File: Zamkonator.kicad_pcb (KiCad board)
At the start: 2 copper layers, 75 x 75 mm, 104 parts, among them J1 Screw_Terminal_01x06, J2 RJ45_Abracon_ARJP11A-MASA-B-A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, J3 Conn_01x08_Male, J4 Conn_02x08_Counter_Clockwise, K1 SRD-DC3V-SL-C, Q1 BCP56, T1 HR051142, U1 RTL8201F, U2 SI3404-A-GM, U3 EL3H7-G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

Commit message: Finish layout
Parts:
- added JP1: SolderJumper_2_Open, Jumper:SolderJumper-2_P1.3mm_Open_RoundedPad1.0x1.5mm, B.Cu at (22.5, 72.8)
- added R32: R, Resistor_SMD:R_0603_1608Metric_Pad0.98x0.95mm_HandSolder, F.Cu at (6.00, 31.2)
- J4: value Conn_02x08_Counter_Clockwise -> Conn_02x06_Counter_Clockwise; footprint Connector_PinHeader_2.54mm:PinHeader_2x08_P2.54mm_Vertical -> Connector_PinHeader_2.54mm:PinHeader_2x06_P2.54mm_Vertical
- moved D9 72.6 mm to (15.0, 62.3), turned to 0 degrees
- moved R2 68.6 mm to (72.3, 31.6)
- moved J1 67.5 mm to (3.60, 35.6), turned to -90 degrees
- moved D8 66.8 mm to (3.50, 55.6)
- moved R1 63.9 mm to (72.2, 33.4), turned to 180 degrees
- moved R29 61.9 mm to (7.70, 52.5), turned to 90 degrees
- moved R28 61.8 mm to (19.2, 45.6), turned to 180 degrees
- moved R30 61.7 mm to (23.4, 54.2), turned to 90 degrees
- moved J_LATCH1 60.7 mm to (4.00, 12.0), turned to -90 degrees
- moved C3 55.6 mm to (66.4, 31.5), turned to 0 degrees
- moved R31 55.1 mm to (10.1, 45.6), turned to 180 degrees
- moved U7 54.0 mm to (15.0, 39.0), turned to 180 degrees
- moved U8 53.2 mm to (15.0, 52.0), turned to 0 degrees
- moved C29 52.7 mm to (25.4, 45.5)
- moved C30 52.7 mm to (30.4, 52.2)
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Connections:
- J1 pad 1: +12V -> /Wigand Intrerface/READER_LED
- J1 pad 2: GND -> /Wigand Intrerface/READER_BUZZER
- J1 pad 5: /Wigand Intrerface/READER_LED -> +12V
- J1 pad 6: /Wigand Intrerface/READER_BUZZER -> GND
- J3 pad 3: /ESP32/IO35 -> /ESP32/IO18
- J4 pad 1: /ESP32/IO2 -> /ESP32/IO12
- J4 pad 10: GND -> /ESP32/IO13
- J4 pad 11: +3.3V -> /ESP32/IO5
- J4 pad 12: +3.3V -> /ESP32/IO4
- J4 pad 2: /50MHZ CLOCK/CLK_EN -> /ESP32/IO2
- J4 pad 3: /ESP32/IO5 -> Net-(J4-Pad3)
- J4 pad 4: /ESP32/IO12 -> +3.3V
- J4 pad 5: /ESP32/IO13 -> +3.3V
- J4 pad 6: /ESP32/IO14 -> GND
- J4 pad 8: /ESP32/IO18 -> /50MHZ CLOCK/CLK_EN
- J4 pad 9: GND -> /ESP32/IO23
- Q1 pad 1: /ESP32/IO35 -> Net-(Q1-Pad1)
- R26 pad 1: /ESP32/IO34 -> /ESP32/IO2
- R27 pad 1: /ESP32/IO33 -> /ESP32/IO12
- R28 pad 2: /ESP32/IO32 -> /ESP32/IO13
- U6 pad 13: /ESP32/IO14 -> /50MHZ CLOCK/CLK_EN
- U6 pad 26: /50MHZ CLOCK/CLK_EN -> /ESP32/IO4
- U6 pad 6: /ESP32/IO34 -> unconnected-(U6-Pad6)
- U6 pad 7: /ESP32/IO35 -> unconnected-(U6-Pad7)
- U6 pad 8: /ESP32/IO32 -> unconnected-(U6-Pad8)
- U6 pad 9: /ESP32/IO33 -> unconnected-(U6-Pad9)
- U8 pad 8: /ESP32/IO32 -> /ESP32/IO13
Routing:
- net GND: track 0.00 -> 89.4 mm, vias 0 -> 58
- net /ESP32/IO12: track 4.76 -> 91.3 mm, vias 1 -> 2
- net /ESP32/IO18: track 10.2 -> 94.8 mm, vias 1 -> 4
- net /ESP32/IO13: track 8.83 -> 83.7 mm, vias 1 -> 6
- net VSS: track 66.2 -> 4.53 mm, vias 2 -> 10
- net /ESP32/IO32: track 61.5 -> 0.00 mm, vias 3 -> 0
- net /ESP32/IO35: track 58.8 -> 0.00 mm, vias 2 -> 0
- net /ESP32/EMAC_CRS_DV: track 62.0 -> 12.3 mm, vias 2 -> 0
- net /ESP32/EMAC_RXD1: track 67.9 -> 24.0 mm, vias 2 -> 0
- net /ESP32/IO2: track 19.1 -> 62.3 mm, vias 1 -> 2
- net +12V: track 172.7 -> 130.5 mm
- net +3.3V: track 218.6 -> 260.5 mm, vias 4 -> 6
- net /50MHZ CLOCK/CLK_OUT: track 90.3 -> 49.5 mm
- net /ESP32/EMAC_RXD0: track 67.4 -> 27.2 mm, vias 2 -> 0
- net Net-(R1-Pad2): track 56.0 -> 16.9 mm
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- added copper zone on B.Cu, net GND
- added copper zone on F.Cu, net GND
- added copper zone on B.Cu, net VSS
- added copper zone on F.Cu, net VSS
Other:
- outline, holes or cut-outs redrawn

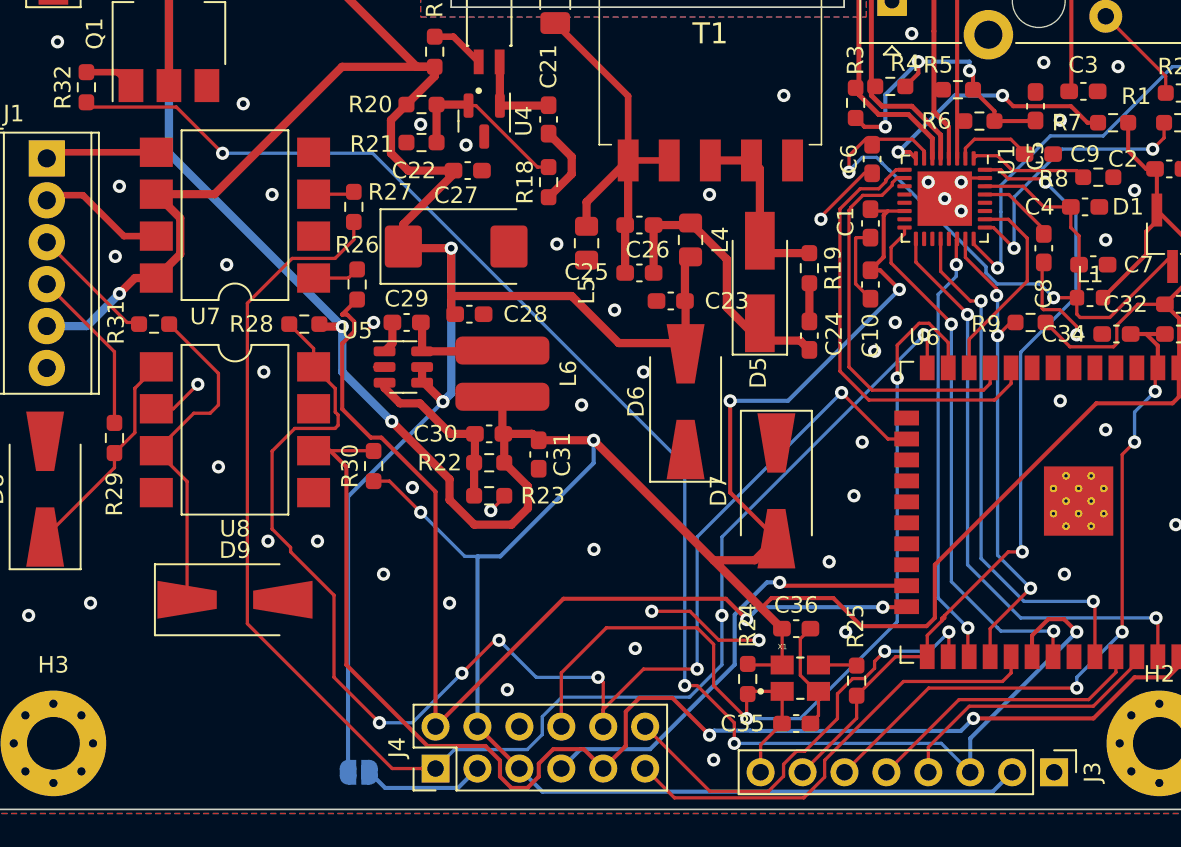
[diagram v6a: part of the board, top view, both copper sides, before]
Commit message: add header labels
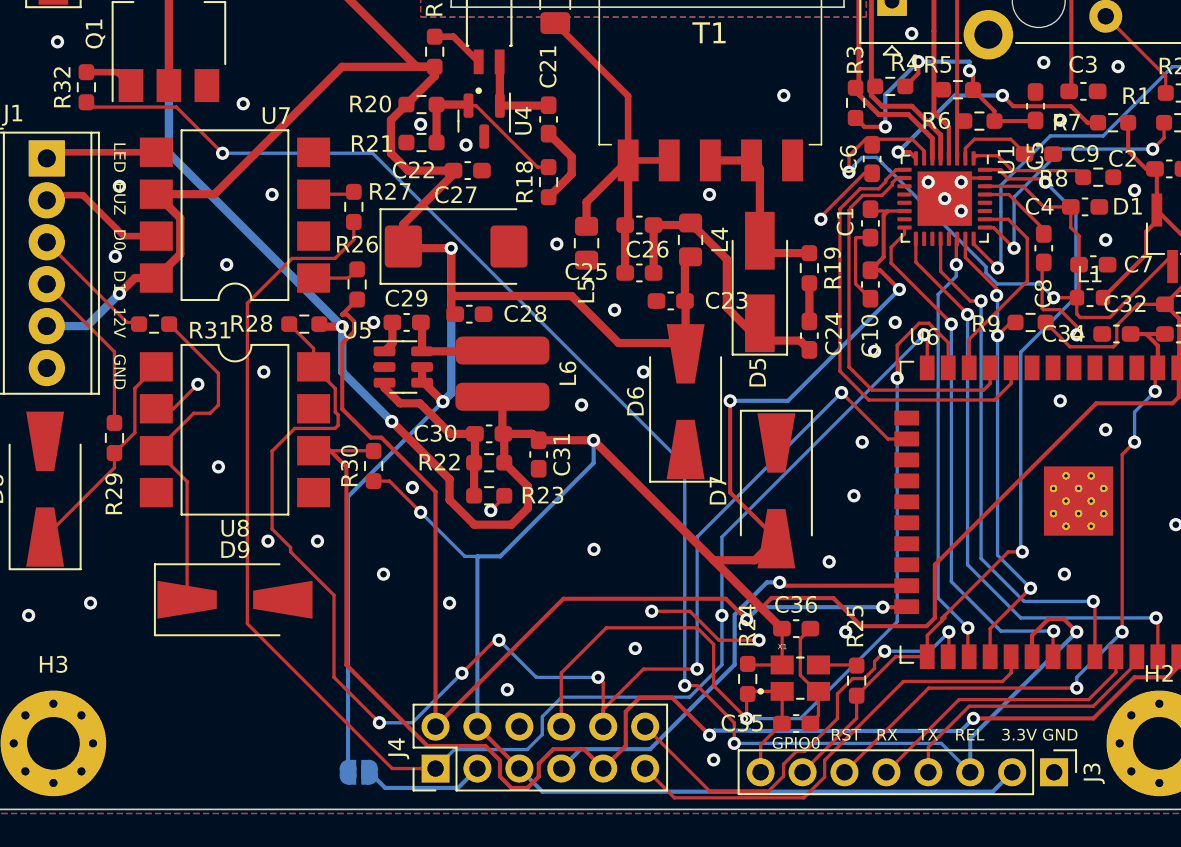
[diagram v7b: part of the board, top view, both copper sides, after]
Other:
- board text added: "12V"
- board text added: "3.3V"
- board text added: "BUZ"
- board text added: "D0"
- board text added: "D1"
- board text added: "GND"
- board text added: "GPIO0"
- board text added: "LED"
- board text added: "REL"
- board text added: "RST"
- board text added: "RX"
- board text added: "TX"
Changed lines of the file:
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@@
     (property "Sheetname" "Wigand Intrerface")
     (attr smd)
-    (fp_text reference "U7" (at 1.8 -6.14) (layer "F.SilkS")
+    (fp_text reference "U7" (at -2.5 6) (layer "F.SilkS")
       (effects (font (size 1 1) (thickness 0.15)))
     )
@@
     (property "Sheetname" "Wigand Intrerface")
     (attr smd)
-    (fp_text reference "R31" (at 2.3 0.1 90) (layer "F.SilkS")
+    (fp_text reference "R31" (at -3.4 -0.4 180) (layer "F.SilkS")
       (effects (font (size 1 1) (thickness 0.15)))
     )
@@
   (gr_rect (start 28.1 25.4) (end 51.9 26.4) (layer "Edge.Cuts") (width 0.1) (fill none))
   (gr_rect (start 0 0) (end 75 75) (layer "Edge.Cuts") (width 0.1) (fill none))
+  (gr_text "RX" (at 54.5 70.5) (layer "F.SilkS")
+    (effects (font (size 0.7 0.7) (thickness 0.15)))
+  )
+  (gr_text "BUZ" (at 8 38 270) (layer "F.SilkS")
+    (effects (font (size 0.7 0.7) (thickness 0.15)))
+  )
+  (gr_text "GND" (at 8 48.5 270) (layer "F.SilkS")
+    (effects (font (size 0.7 0.7) (thickness 0.15)))
+  )
+  (gr_text "TX" (at 57 70.5) (layer "F.SilkS")
+    (effects (font (size 0.7 0.7) (thickness 0.15)))
+  )
+  (gr_text "D0" (at 8 40.5 270) (layer "F.SilkS")
+    (effects (font (size 0.7 0.7) (thickness 0.15)))
+  )
+  (gr_text "LED" (at 8 35.5 270) (layer "F.SilkS")
+    (effects (font (size 0.7 0.7) (thickness 0.15)))
+  )
+  (gr_text "D1" (at 8 43 270) (layer "F.SilkS")
+    (effects (font (size 0.7 0.7) (thickness 0.15)))
+  )
+  (gr_text "GPIO0" (at 49 71) (layer "F.SilkS")
+    (effects (font (size 0.7 0.7) (thickness 0.15)))
+  )
+  (gr_text "3.3V" (at 62.5 70.5) (layer "F.SilkS")
+    (effects (font (size 0.7 0.7) (thickness 0.15)))
+  )
+  (gr_text "REL" (at 59.5 70.5) (layer "F.SilkS")
+    (effects (font (size 0.7 0.7) (thickness 0.15)))
+  )
+  (gr_text "GND" (at 65 70.5) (layer "F.SilkS")
+    (effects (font (size 0.7 0.7) (thickness 0.15)))
+  )
+  (gr_text "RST" (at 52 70.5) (layer "F.SilkS")
+    (effects (font (size 0.7 0.7) (thickness 0.15)))
+  )
+  (gr_text "12V" (at 8 45.5 270) (layer "F.SilkS")
+    (effects (font (size 0.7 0.7) (thickness 0.15)))
+  )
   (segment (start 59.5 16) (end 60.645 14.855) (width 0.5) (layer "F.Cu") (net 1))
   (segment (start 63.9 44.65) (end 63.975 44.725) (width 0.2) (layer "F.Cu") (net 1))

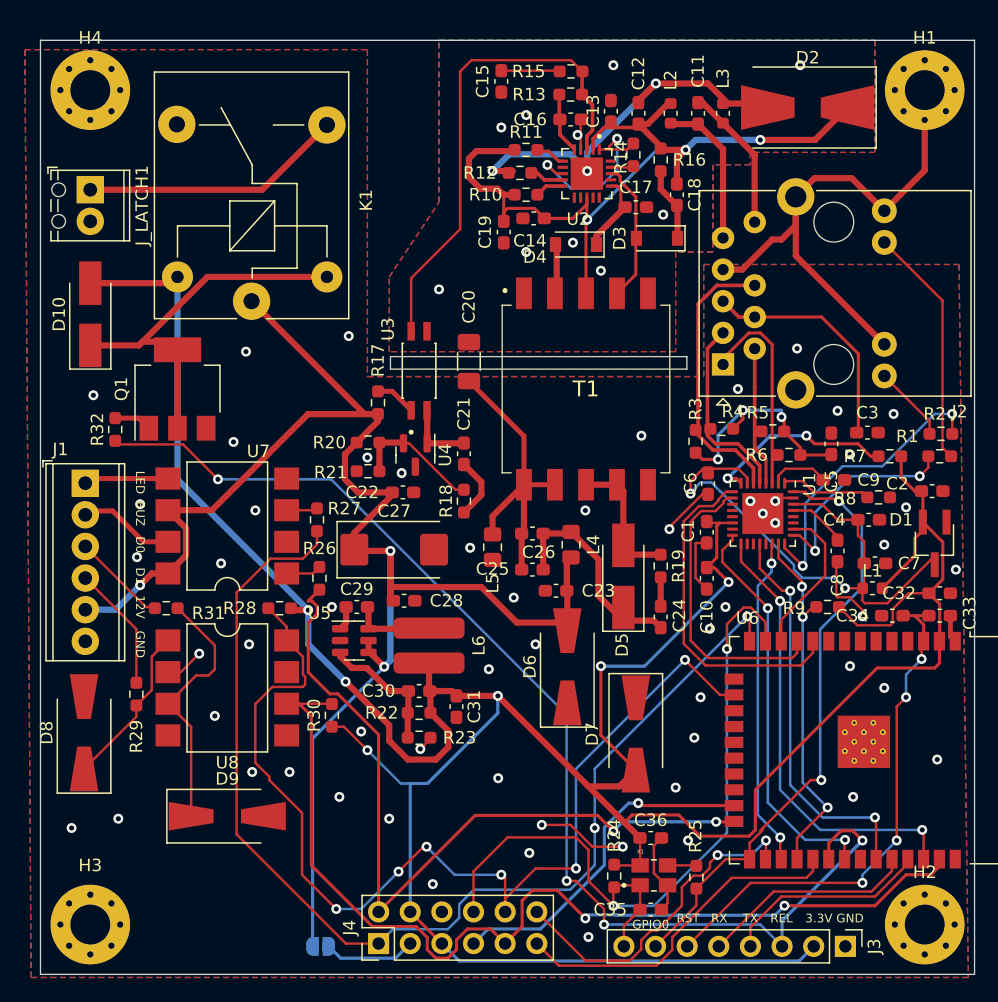
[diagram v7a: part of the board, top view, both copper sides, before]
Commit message: Add testpoints, jumpers
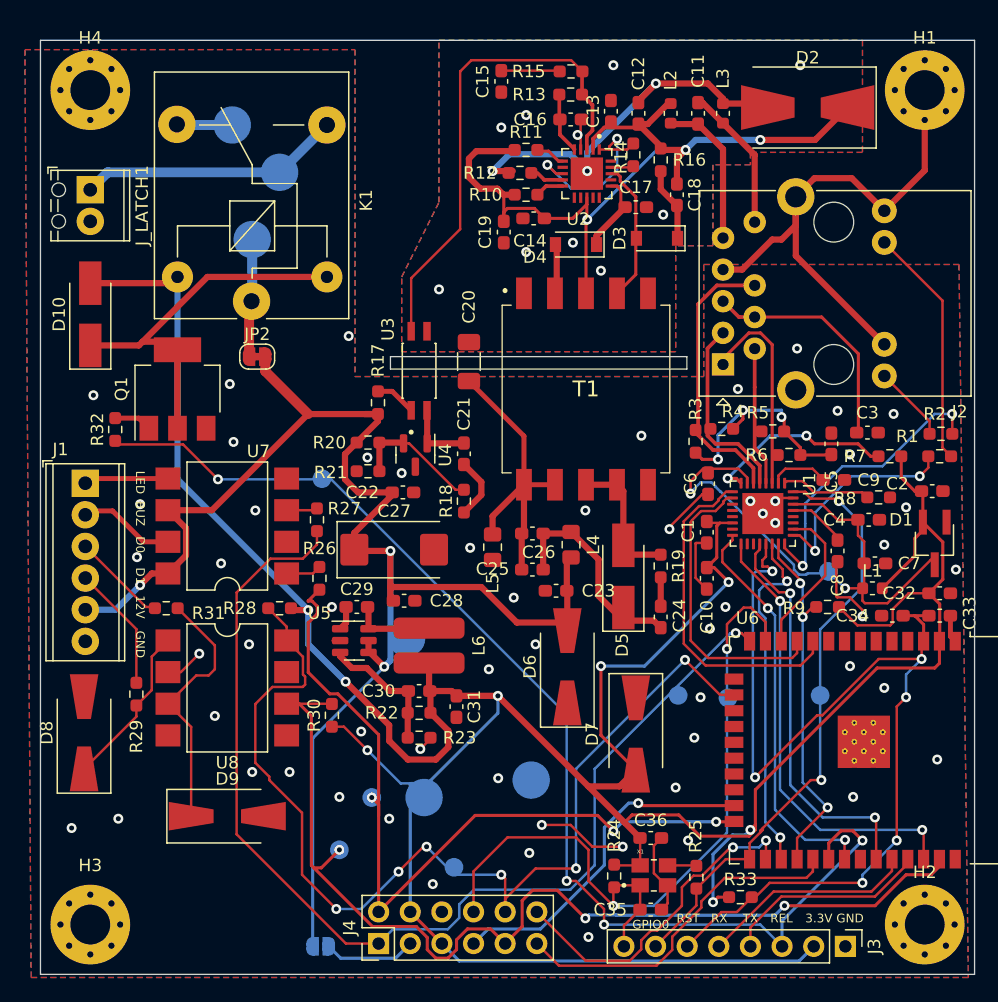
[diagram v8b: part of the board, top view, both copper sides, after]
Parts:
- added JP2: SolderJumper_2_Bridged, Jumper:SolderJumper-2_P1.3mm_Bridged_RoundedPad1.0x1.5mm, F.Cu at (17.4, 25.4)
- added R33: 10k, Resistor_SMD:R_0603_1608Metric_Pad0.98x0.95mm_HandSolder, F.Cu at (56.2, 68.8)
- added TP1: TestPoint, TestPoint:TestPoint_Pad_D3.0mm, B.Cu at (39.4, 59.4)
- added TP10: TestPoint, TestPoint:TestPoint_Pad_D1.5mm, B.Cu at (26.6, 60.8)
- added TP11: TestPoint, TestPoint:TestPoint_Pad_D1.5mm, B.Cu at (24.0, 65.0)
- added TP12: TestPoint, TestPoint:TestPoint_Pad_D3.0mm, B.Cu at (19.2, 10.6)
- added TP13: TestPoint, TestPoint:TestPoint_Pad_D3.0mm, B.Cu at (15.4, 6.80)
- added TP14: TestPoint, TestPoint:TestPoint_Pad_D3.0mm, B.Cu at (17.0, 16.0)
- added TP2: TestPoint, TestPoint:TestPoint_Pad_D3.0mm, B.Cu at (29.4, 48.0)
- added TP3: TestPoint, TestPoint:TestPoint_Pad_D1.5mm, B.Cu at (62.6, 52.6)
- added TP4: TestPoint, TestPoint:TestPoint_Pad_D1.5mm, B.Cu at (22.6, 35.2)
- added TP5: TestPoint, TestPoint:TestPoint_Pad_D1.5mm, B.Cu at (63.3, 42.6)
- added TP6: TestPoint, TestPoint:TestPoint_Pad_D3.0mm, B.Cu at (30.8, 60.8)
- added TP7: TestPoint, TestPoint:TestPoint_Pad_D1.5mm, B.Cu at (55.2, 52.8)
- added TP8: TestPoint, TestPoint:TestPoint_Pad_D1.5mm, B.Cu at (51.2, 52.6)
- added TP9: TestPoint, TestPoint:TestPoint_Pad_D1.5mm, B.Cu at (33.2, 66.4)
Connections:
- K1 pad 1: +12V -> /Relay/C
- U1 pad 21: /Ethenet PHY/EMAC_EN -> /ESP32/ESP_EN
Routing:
- net /ESP32/ESP_EN: track 42.0 -> 80.3 mm, vias 4 -> 6
- net +3.3V: track 260.5 -> 270.1 mm, vias 6 -> 8
- net /Relay/C: track 0.00 -> 9.50 mm
- net +12V: track 130.5 -> 123.8 mm
- net /Relay/NC: track 0.00 -> 4.47 mm
- net /ESP32/IO23: track 80.3 -> 82.9 mm, vias 2 -> 3
- net /ESP32/IO12: track 91.3 -> 89.1 mm, vias 2 -> 1
- net /ESP32/EMAC_MDC: track 26.6 -> 28.4 mm
- net /ESP32/IO2: track 62.3 -> 64.0 mm, vias 2 -> 3
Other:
- board text added: "RELAY"
